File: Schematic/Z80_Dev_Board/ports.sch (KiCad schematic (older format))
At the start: 15 parts, among them J1 MCU Interface, J2 Expansion port, J3 MCU Interface 2, J4 GPIO, J5 UART B, J6 UART A, U9 SC26C92, Y1 3,6864 MHz

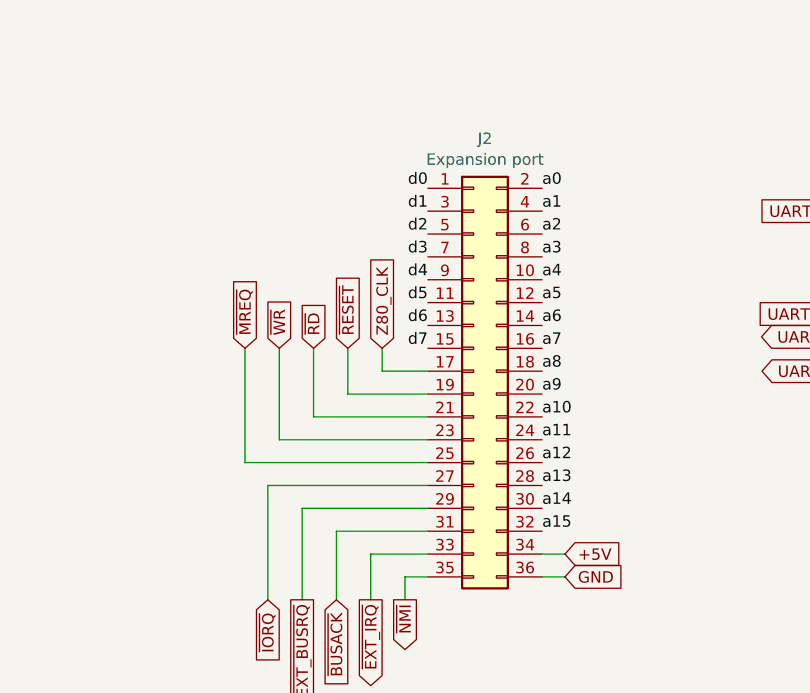
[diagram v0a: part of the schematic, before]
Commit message: Added global bus labels
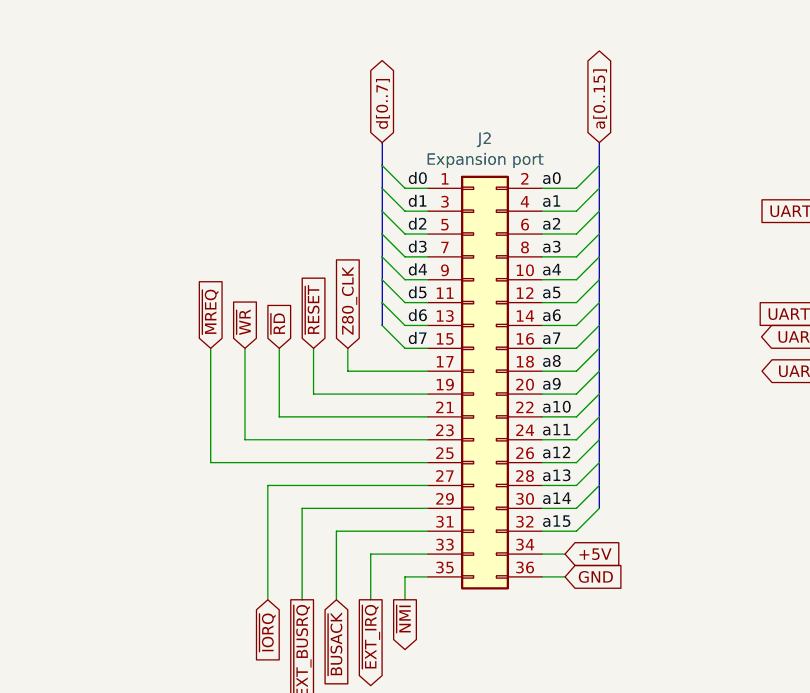
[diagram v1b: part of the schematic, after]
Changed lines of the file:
@@
 Text Label 5700 2450 2    50   ~ 0
 d7
-Text GLabel 5500 2450 1    50   Input ~ 0
+Text GLabel 5350 2450 1    50   Input ~ 0
 Z80_CLK
-Text GLabel 5350 2450 1    50   Input ~ 0
+Text GLabel 5200 2450 1    50   Input ~ 0
 ~RESET
 Wire Wire Line
-	5350 2450 5350 2650
-Wire Wire Line
-	5350 2650 5700 2650
-Wire Wire Line
-	5500 2450 5500 2550
-Wire Wire Line
-	5500 2550 5700 2550
-Text GLabel 5200 2450 1    50   Input ~ 0
+	5200 2450 5200 2650
+Wire Wire Line
+	5200 2650 5700 2650
+Wire Wire Line
+	5350 2450 5350 2550
+Wire Wire Line
+	5350 2550 5700 2550
+Text GLabel 5050 2450 1    50   Input ~ 0
 ~RD
 Wire Wire Line
-	5200 2450 5200 2750
-Wire Wire Line
-	5200 2750 5700 2750
-Text GLabel 5050 2450 1    50   Input ~ 0
+	5050 2450 5050 2750
+Wire Wire Line
+	5050 2750 5700 2750
+Text GLabel 4900 2450 1    50   Input ~ 0
 ~WR
 Wire Wire Line
-	5050 2450 5050 2850
-Wire Wire Line
-	5050 2850 5700 2850
-Text GLabel 4900 2450 1    50   Input ~ 0
+	4900 2450 4900 2850
+Wire Wire Line
+	4900 2850 5700 2850
+Text GLabel 4750 2450 1    50   Input ~ 0
 ~MREQ
 Wire Wire Line
-	4900 2450 4900 2950
-Wire Wire Line
-	4900 2950 5700 2950
+	4750 2450 4750 2950
+Wire Wire Line
+	4750 2950 5700 2950
 Text GLabel 5000 3550 3    50   Input ~ 0
 ~IORQ
@@
 Wire Wire Line
 	2950 3050 3250 3050
+Entry Wire Line
+	5500 1650 5600 1750
+Entry Wire Line
+	5500 1750 5600 1850
+Entry Wire Line
+	5500 1850 5600 1950
+Entry Wire Line
+	5500 1950 5600 2050
+Entry Wire Line
+	5500 2050 5600 2150
+Entry Wire Line
+	5500 2150 5600 2250
+Entry Wire Line
+	5500 2250 5600 2350
+Entry Wire Line
+	5500 2350 5600 2450
+Wire Wire Line
+	5600 2450 5700 2450
+Wire Wire Line
+	5600 2350 5700 2350
+Wire Wire Line
+	5600 2250 5700 2250
+Wire Wire Line
+	5600 2150 5700 2150
+Wire Wire Line
+	5600 2050 5700 2050
+Wire Wire Line
+	5600 1950 5700 1950
+Wire Wire Line
+	5600 1850 5700 1850
+Wire Wire Line
+	5600 1750 5700 1750
+Entry Wire Line
+	6350 1750 6450 1650
+Entry Wire Line
+	6350 1850 6450 1750
+Entry Wire Line
+	6350 1950 6450 1850
+Entry Wire Line
+	6350 2050 6450 1950
+Entry Wire Line
+	6350 2150 6450 2050
+Entry Wire Line
+	6350 2250 6450 2150
+Entry Wire Line
+	6350 2350 6450 2250
+Entry Wire Line
+	6350 2450 6450 2350
+Entry Wire Line
+	6350 2550 6450 2450
+Entry Wire Line
+	6350 2650 6450 2550
+Entry Wire Line
+	6350 2750 6450 2650
+Entry Wire Line
+	6350 2850 6450 2750
+Entry Wire Line
+	6350 2950 6450 2850
+Entry Wire Line
+	6350 3050 6450 2950
+Entry Wire Line
+	6350 3150 6450 3050
+Entry Wire Line
+	6350 3250 6450 3150
+Wire Wire Line
+	6350 3250 6200 3250
+Wire Wire Line
+	6200 3150 6350 3150
+Wire Wire Line
+	6200 3050 6350 3050
+Wire Wire Line
+	6200 2950 6350 2950
+Wire Wire Line
+	6200 2850 6350 2850
+Wire Wire Line
+	6200 2750 6350 2750
+Wire Wire Line
+	6200 2650 6350 2650
+Wire Wire Line
+	6200 2550 6350 2550
+Wire Wire Line
+	6200 2450 6350 2450
+Wire Wire Line
+	6200 2350 6350 2350
+Wire Wire Line
+	6200 2250 6350 2250
+Wire Wire Line
+	6200 2150 6350 2150
+Wire Wire Line
+	6200 2050 6350 2050
+Wire Wire Line
+	6200 1950 6350 1950
+Wire Wire Line
+	6200 1850 6350 1850
+Wire Wire Line
+	6200 1750 6350 1750
+Text GLabel 5500 1550 1    50   BiDi ~ 0
+d[0..7]
+Text GLabel 6450 1550 1    50   BiDi ~ 0
+a[0..15]
+Wire Bus Line
+	5500 1550 5500 2350
+Wire Bus Line
+	6450 1550 6450 3150
 $EndSCHEMATC

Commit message: PCB RC1
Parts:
- added TP1: TestPoint, TestPoint:TestPoint_Keystone_5005-5009_Compact, symbol Connector:TestPoint
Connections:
- net GND: now also TP1.1
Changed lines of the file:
@@
 Text GLabel 6450 1550 1    50   BiDi ~ 0
 a[0..15]
+$Comp
+L Connector:TestPoint TP1
+U 1 1 5FB6421F
+P 4200 3400
+F 0 "TP1" H 4258 3518 50  0000 L CNN
+F 1 "TestPoint" H 4258 3427 50  0000 L CNN
+F 2 "TestPoint:TestPoint_Keystone_5005-5009_Compact" H 4400 3400 50  0001 C CNN
+F 3 "~" H 4400 3400 50  0001 C CNN
+	1    4200 3400
+	1    0    0    -1
+$EndComp
+Text GLabel 4200 3500 3    50   Input ~ 0
+GND
+Wire Wire Line
+	4200 3500 4200 3400
 Wire Bus Line
 	5500 1550 5500 2350

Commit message: Completed PCB rework
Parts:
- J2: footprint Connector_PinHeader_2.54mm:PinHeader_2x18_P2.54mm_Vertical -> Connector_PinSocket_2.54mm:PinSocket_2x18_P2.54mm_Vertical
- J3: footprint Connector_PinHeader_2.54mm:PinHeader_1x08_P2.54mm_Vertical -> Connector_PinSocket_2.54mm:PinSocket_1x08_P2.54mm_Vertical
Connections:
- net +5V: now also J2.33 (Pin_33); no longer J2.34 (Pin_34)
- net CLKSEL: now also J1.20 (Pin_20); no longer J1.19 (Pin_19)
- net DBG_CLK: now also J1.33 (Pin_33); no longer J1.34 (Pin_34)
- net GND: now also J2.35 (Pin_35); no longer J2.36 (Pin_36)
- net Z80_CLK: now also J2.18 (Pin_18); no longer J2.17 (Pin_17)
- net a0: now also J1.4 (Pin_4), J2.1 (Pin_1); no longer J1.3 (Pin_3), J2.2 (Pin_2)
- net a1: now also J1.3 (Pin_3), J2.3 (Pin_3); no longer J1.4 (Pin_4), J2.4 (Pin_4)
- net a10: now also J1.15 (Pin_15), J2.21 (Pin_21); no longer J1.16 (Pin_16), J2.22 (Pin_22)
- net a11: now also J1.16 (Pin_16), J2.23 (Pin_23); no longer J1.15 (Pin_15), J2.24 (Pin_24)
- net a12: now also J1.13 (Pin_13), J2.25 (Pin_25); no longer J1.14 (Pin_14), J2.26 (Pin_26)
- net a13: now also J1.14 (Pin_14), J2.27 (Pin_27); no longer J1.13 (Pin_13), J2.28 (Pin_28)
- net a14: now also J1.11 (Pin_11), J2.29 (Pin_29); no longer J1.12 (Pin_12), J2.30 (Pin_30)
- net a15: now also J1.12 (Pin_12), J2.31 (Pin_31); no longer J1.11 (Pin_11), J2.32 (Pin_32)
- net a2: now also J1.6 (Pin_6), J2.5 (Pin_5); no longer J1.5 (Pin_5), J2.6 (Pin_6)
- net a3: now also J1.5 (Pin_5), J2.7 (Pin_7); no longer J1.6 (Pin_6), J2.8 (Pin_8)
- net a4: now also J1.8 (Pin_8), J2.9 (Pin_9); no longer J1.7 (Pin_7), J2.10 (Pin_10)
- net a5: now also J1.7 (Pin_7), J2.11 (Pin_11); no longer J1.8 (Pin_8), J2.12 (Pin_12)
- net a6: now also J1.10 (Pin_10), J2.13 (Pin_13); no longer J1.9 (Pin_9), J2.14 (Pin_14)
- net a7: now also J1.9 (Pin_9), J2.15 (Pin_15); no longer J1.10 (Pin_10), J2.16 (Pin_16)
- net a8: now also J1.17 (Pin_17), J2.17 (Pin_17); no longer J1.18 (Pin_18), J2.18 (Pin_18)
- net a9: now also J1.18 (Pin_18), J2.19 (Pin_19); no longer J1.17 (Pin_17), J2.20 (Pin_20)
- net d0: now also J1.29 (Pin_29), J2.2 (Pin_2); no longer J1.30 (Pin_30), J2.1 (Pin_1)
- net d1: now also J1.30 (Pin_30), J2.4 (Pin_4); no longer J1.29 (Pin_29), J2.3 (Pin_3)
- net d2: now also J1.27 (Pin_27), J2.6 (Pin_6); no longer J1.28 (Pin_28), J2.5 (Pin_5)
- net d3: now also J1.28 (Pin_28), J2.8 (Pin_8); no longer J1.27 (Pin_27), J2.7 (Pin_7)
- net d4: now also J1.25 (Pin_25), J2.10 (Pin_10); no longer J1.26 (Pin_26), J2.9 (Pin_9)
- net d5: now also J1.26 (Pin_26), J2.12 (Pin_12); no longer J1.25 (Pin_25), J2.11 (Pin_11)
- net d6: now also J1.23 (Pin_23), J2.14 (Pin_14); no longer J1.24 (Pin_24), J2.13 (Pin_13)
- net d7: now also J1.24 (Pin_24), J2.16 (Pin_16); no longer J1.23 (Pin_23), J2.15 (Pin_15)
- net ~BUSACK: now also J2.32 (Pin_32); no longer J2.31 (Pin_31)
- net ~DBG_BUSRQ: now also J1.34 (Pin_34); no longer J1.33 (Pin_33)
- net ~EXT_BUSRQ: now also J2.30 (Pin_30); no longer J2.29 (Pin_29)
- net ~EXT_IRQ: now also J2.34 (Pin_34); no longer J2.33 (Pin_33)
- net ~IORQ: now also J2.28 (Pin_28); no longer J2.27 (Pin_27)
- net ~MREQ: now also J2.26 (Pin_26); no longer J2.25 (Pin_25)
- net ~NMI: now also J2.36 (Pin_36); no longer J2.35 (Pin_35)
- net ~RD: now also J2.22 (Pin_22); no longer J2.21 (Pin_21)
- net ~RESET: now also J1.32 (Pin_32), J2.20 (Pin_20); no longer J1.31 (Pin_31), J2.19 (Pin_19)
- net ~WAIT: now also J1.31 (Pin_31); no longer J1.32 (Pin_32)
- net ~WR: now also J2.24 (Pin_24); no longer J2.23 (Pin_23)
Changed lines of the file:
@@
 Comment4 "Created by Dawid Buchwald"
 $EndDescr
-$Comp
-L Connector_Generic:Conn_02x18_Odd_Even J1
-U 1 1 5FB78A65
-P 2350 2200
-F 0 "J1" H 2400 3217 50  0000 C CNN
-F 1 "MCU Interface" H 2400 3126 50  0000 C CNN
-F 2 "Connector_PinHeader_2.54mm:PinHeader_2x18_P2.54mm_Vertical" H 2350 2200 50  0001 C CNN
-F 3 "~" H 2350 2200 50  0001 C CNN
-	1    2350 2200
-	1    0    0    -1
-$EndComp
 Text GLabel 2050 1300 1    50   Input ~ 0
 +5V
@@
 	1900 3050 1900 3000
 Wire Wire Line
-	1900 3000 2150 3000
+	1900 3000 2050 3000
 Wire Wire Line
 	3250 2900 3150 2900
@@
 	1800 2900 1900 2900
 Wire Wire Line
-	1900 2900 2150 2900
+	1900 2900 2050 2900
 Text GLabel 1800 3050 0    50   Output ~ 0
 ~DBG_BUSRQ
@@
 	1800 2300 1900 2300
 Wire Wire Line
-	1900 2300 2150 2300
+	1900 2300 2050 2300
 Text GLabel 3250 2900 2    50   Output ~ 0
 ~WAIT
@@
 F 0 "J3" H 3000 5400 50  0000 C CNN
 F 1 "MCU Interface 2" V 3100 4600 50  0000 L CNN
-F 2 "Connector_PinHeader_2.54mm:PinHeader_1x08_P2.54mm_Vertical" H 3000 4950 50  0001 C CNN
+F 2 "Connector_PinSocket_2.54mm:PinSocket_1x08_P2.54mm_Vertical" H 3000 4950 50  0001 C CNN
 F 3 "~" H 3000 4950 50  0001 C CNN
 	1    3000 4950
@@
 L Connector_Generic:Conn_02x18_Odd_Even J?
 U 1 1 5FBB88CB
-P 5900 2550
+P 6000 2550
 AR Path="/5FBB88CB" Ref="J?"  Part="1"
 AR Path="/5FB5970D/5FBB88CB" Ref="J2"  Part="1"
-F 0 "J2" H 5950 3567 50  0000 C CNN
-F 1 "Expansion port" H 5950 3476 50  0000 C CNN
-F 2 "Connector_PinHeader_2.54mm:PinHeader_2x18_P2.54mm_Vertical" H 5900 2550 50  0001 C CNN
-F 3 "~" H 5900 2550 50  0001 C CNN
-	1    5900 2550
-	1    0    0    -1
+F 0 "J2" H 6050 3567 50  0000 C CNN
+F 1 "Expansion port" H 6050 3476 50  0000 C CNN
+F 2 "Connector_PinSocket_2.54mm:PinSocket_2x18_P2.54mm_Vertical" H 6000 2550 50  0001 C CNN
+F 3 "~" H 6000 2550 50  0001 C CNN
+	1    6000 2550
+	-1   0    0    -1
 $EndComp
 Text Label 6200 1750 0    50   ~ 0
@@
 Wire Wire Line
 	4200 3500 4200 3400
+$Comp
+L Connector_Generic:Conn_02x18_Odd_Even J1
+U 1 1 5FB78A65
+P 2450 2200
+F 0 "J1" H 2500 3217 50  0000 C CNN
+F 1 "MCU Interface" H 2500 3126 50  0000 C CNN
+F 2 "Connector_PinHeader_2.54mm:PinHeader_2x18_P2.54mm_Vertical" H 2450 2200 50  0001 C CNN
+F 3 "~" H 2450 2200 50  0001 C CNN
+	1    2450 2200
+	-1   0    0    -1
+$EndComp
+Connection ~ 2050 1400
+Connection ~ 2050 2300
+Wire Wire Line
+	2050 2300 2150 2300
+Connection ~ 2050 2900
+Wire Wire Line
+	2050 2900 2150 2900
+Connection ~ 2050 3000
+Wire Wire Line
+	2050 3000 2150 3000
+Connection ~ 2050 3100
 Wire Bus Line
 	5500 1550 5500 2350

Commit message: PCB RC3 with gerbers
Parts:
- added J7: GPIO Output, Connector_PinSocket_2.54mm:PinSocket_1x06_P2.54mm_Vertical, symbol Connector_Generic:Conn_01x06
- J6: renamed from J4; value GPIO -> GPIO Input; footprint Connector_PinSocket_2.54mm:PinSocket_1x11_P2.54mm_Vertical -> Connector_PinSocket_2.54mm:PinSocket_1x05_P2.54mm_Vertical; symbol Connector_Generic:Conn_01x11 -> Connector_Generic:Conn_01x05
- renumbered J3 to J2, J2 to J3, J5 to J4, J6 to J5
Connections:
- net op2: now also J7.1 (Pin_1); no longer J6.6 (Pin_6)
- net op3: now also J7.2 (Pin_2); no longer J6.7 (Pin_7)
- net op4: now also J7.3 (Pin_3); no longer J6.8 (Pin_8)
- net op5: now also J7.4 (Pin_4); no longer J6.9 (Pin_9)
- net op6: now also J7.5 (Pin_5); no longer J6.10 (Pin_10)
- net op7: now also J7.6 (Pin_6); no longer J6.11 (Pin_11)
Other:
- moved on the sheet: C11, C12, C13, J2, J3, J4, J5, U9, Y1

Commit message: New version of the board created
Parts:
- removed J3: Expansion port, Connector_PinSocket_2.54mm:PinSocket_2x18_P2.54mm_Vertical, symbol Connector_Generic:Conn_02x18_Odd_Even
- removed J6: GPIO Input, Connector_PinSocket_2.54mm:PinSocket_1x05_P2.54mm_Vertical, symbol Connector_Generic:Conn_01x05
- removed J7: GPIO Output, Connector_PinSocket_2.54mm:PinSocket_1x06_P2.54mm_Vertical, symbol Connector_Generic:Conn_01x06
- removed R10, R7, R8, R9: 4K7, Resistor_THT:R_Axial_DIN0207_L6.3mm_D2.5mm_P10.16mm_Horizontal, symbol Device:R
- added J5: Extension Bus, Connector_PinSocket_2.54mm:PinSocket_2x32_P2.54mm_Vertical, symbol Connector_Generic:Conn_02x32_Odd_Even
- added RN1, RN2: 4K7, Resistor_THT:R_Array_SIP9, symbol Device:R_Network08
- C12: renamed from C11; footprint Capacitor_THT:C_Disc_D5.0mm_W2.5mm_P2.50mm -> Capacitor_SMD:C_1206_3216Metric_Pad1.42x1.75mm_HandSolder
- renumbered C12 to C13, C13 to C14, J4 to J3, J5 to J4, U9 to U10
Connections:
- net +5V: now also J5.1 (Pin_1), J5.2 (Pin_2), J5.61 (Pin_61), J5.62 (Pin_62), RN2.1 (common)
- net CLKSEL: now also RN1.3 (R2)
- net DBG_CLK: now also RN1.4 (R3)
- net GND: now also J5.3 (Pin_3), J5.4 (Pin_4), J5.63 (Pin_63), J5.64 (Pin_64), RN1.1 (common)
- net Z80_CLK: now also J5.22 (Pin_22)
- net a0: now also J5.5 (Pin_5)
- net a1: now also J5.7 (Pin_7)
- net a10: now also J5.25 (Pin_25)
- net a11: now also J5.27 (Pin_27)
- net a12: now also J5.29 (Pin_29)
- net a13: now also J5.31 (Pin_31)
- net a14: now also J5.33 (Pin_33)
- net a15: now also J5.35 (Pin_35)
- net a2: now also J5.9 (Pin_9)
- net a3: now also J5.11 (Pin_11)
- net a4: now also J5.13 (Pin_13)
- net a5: now also J5.15 (Pin_15)
- net a6: now also J5.17 (Pin_17)
- net a7: now also J5.19 (Pin_19)
- net a8: now also J5.21 (Pin_21)
- net a9: now also J5.23 (Pin_23)
- net d0: now also J5.6 (Pin_6)
- net d1: now also J5.8 (Pin_8)
- net d2: now also J5.10 (Pin_10)
- net d3: now also J5.12 (Pin_12)
- net d4: now also J5.14 (Pin_14)
- net d5: now also J5.16 (Pin_16)
- net d6: now also J5.18 (Pin_18)
- net d7: now also J5.20 (Pin_20)
- net ip2: now also J5.37 (Pin_37), RN1.5 (R4)
- net ip3: now also J5.39 (Pin_39), RN1.6 (R5)
- net ip4: now also J5.41 (Pin_41), RN1.7 (R6)
- net ip5: now also J5.43 (Pin_43), RN1.8 (R7)
- net ip6: now also J5.45 (Pin_45), RN1.9 (R8)
- net op2: now also J5.47 (Pin_47)
- net op3: now also J5.49 (Pin_49)
- net op4: now also J5.51 (Pin_51)
- net op5: now also J5.53 (Pin_53)
- net op6: now also J5.55 (Pin_55)
- net op7: now also J5.57 (Pin_57)
- net ~BUSACK: now also J5.36 (Pin_36)
- net ~DBG_BUSRQ: now also RN2.6 (R5)
- net ~EXT_BUSRQ: now also J5.34 (Pin_34), RN2.7 (R6)
- net ~EXT_IRQ: now also J5.38 (Pin_38), RN2.5 (R4)
- net ~IORQ: now also J5.32 (Pin_32)
- net ~M1: now also J5.56 (Pin_56)
- net ~MREQ: now also J5.30 (Pin_30)
- net ~NMI: now also J5.40 (Pin_40), RN2.3 (R2)
- net ~RD: now also J5.26 (Pin_26)
- net ~RESET: now also J5.24 (Pin_24), RN1.2 (R1)
- net ~UART_IRQ: now also RN2.4 (R3)
- net ~WAIT: now also RN2.2 (R1)
- net ~WR: now also J5.28 (Pin_28)
- net mc1: now reaches J1.19 (Pin_19)
- net mc1: now also J5.59 (Pin_59)
- net mc2: now reaches J1.21 (Pin_21)
- net mc2: now also J5.60 (Pin_60)
- net mc3: now reaches J1.22 (Pin_22)
- net mc3: now also J5.58 (Pin_58)
- new net ~IO1: J5.42 (Pin_42)
- new net ~IO2: J5.44 (Pin_44)
- new net ~IO3: J5.46 (Pin_46)
- new net ~IO4: J5.48 (Pin_48)
- new net ~IO5: J5.50 (Pin_50)
- new net ~IO6: J5.52 (Pin_52)
- new net ~IO7: J5.54 (Pin_54)
- no-connect marks 5 -> 4
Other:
- moved on the sheet: C12, C13, C14, U10, Y1

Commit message: Replaced THT caps/resistors with SMD
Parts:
- C13, C14: footprint Capacitor_THT:C_Disc_D5.0mm_W2.5mm_P2.50mm -> Capacitor_SMD:C_1206_3216Metric_Pad1.33x1.80mm_HandSolder
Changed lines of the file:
@@
 F 0 "C13" H 5700 5900 50  0000 L CNN
 F 1 "22pF" H 5700 5800 50  0000 L CNN
-F 2 "Capacitor_THT:C_Disc_D5.0mm_W2.5mm_P2.50mm" H 5600 5850 50  0001 C CNN
+F 2 "Capacitor_SMD:C_1206_3216Metric_Pad1.33x1.80mm_HandSolder" H 5600 5850 50  0001 C CNN
 F 3 "~" H 5600 5850 50  0001 C CNN
 	1    5600 5850
@@
 F 0 "C14" H 5700 6600 50  0000 L CNN
 F 1 "22pF" H 5700 6500 50  0000 L CNN
-F 2 "Capacitor_THT:C_Disc_D5.0mm_W2.5mm_P2.50mm" H 5600 6550 50  0001 C CNN
+F 2 "Capacitor_SMD:C_1206_3216Metric_Pad1.33x1.80mm_HandSolder" H 5600 6550 50  0001 C CNN
 F 3 "~" H 5600 6550 50  0001 C CNN
 	1    5600 6550

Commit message: Last-minute updates to board layout (and clock toggle schematic)
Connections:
- net Z80_CLK renamed ~Z80_CLK
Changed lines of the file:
@@
 d7
 Text GLabel 8600 3000 1    50   Input ~ 0
-Z80_CLK
+~Z80_CLK
 Text GLabel 8450 3000 1    50   Input ~ 0
 ~RESET
